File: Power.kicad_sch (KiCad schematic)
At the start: 19 parts, among them U1 SY8089AAAC, U2 SGM2048-ADJXTEK8G/TR

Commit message: Global label modified
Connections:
- net +3V3 renamed +3V3 main
- net +3V3 main: no longer C8.1, R7.2, U2.1 (OUT), U2.2 (OUT)
- new net +3V3 sens: C8.1, R7.2, U2.1 (OUT), U2.2 (OUT)
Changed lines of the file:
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@@
-		)
-	)
-	(label "Vout-Sens"
-		(at 214.63 96.52 0)
-		(effects
-			(font
-				(size 1.27 1.27)
-			)
-			(justify left bottom)
-		)
-	)
-	(label "Vout-Main"
-		(at 218.44 46.99 0)
-		(effects
-			(font
-				(size 1.27 1.27)
-			)
-			(justify left bottom)
 		)
 	)
@@
 			)
 		)
-		(property "Value" "+3V3"
+		(property "Value" "+3V3 main"
 			(at 218.44 48.2599 90)
 			(show_name no)
@@
 			)
 		)
-		(property "Value" "+3V3"
+		(property "Value" "+3V3 sens"
 			(at 217.17 99.0599 90)
 			(show_name no)

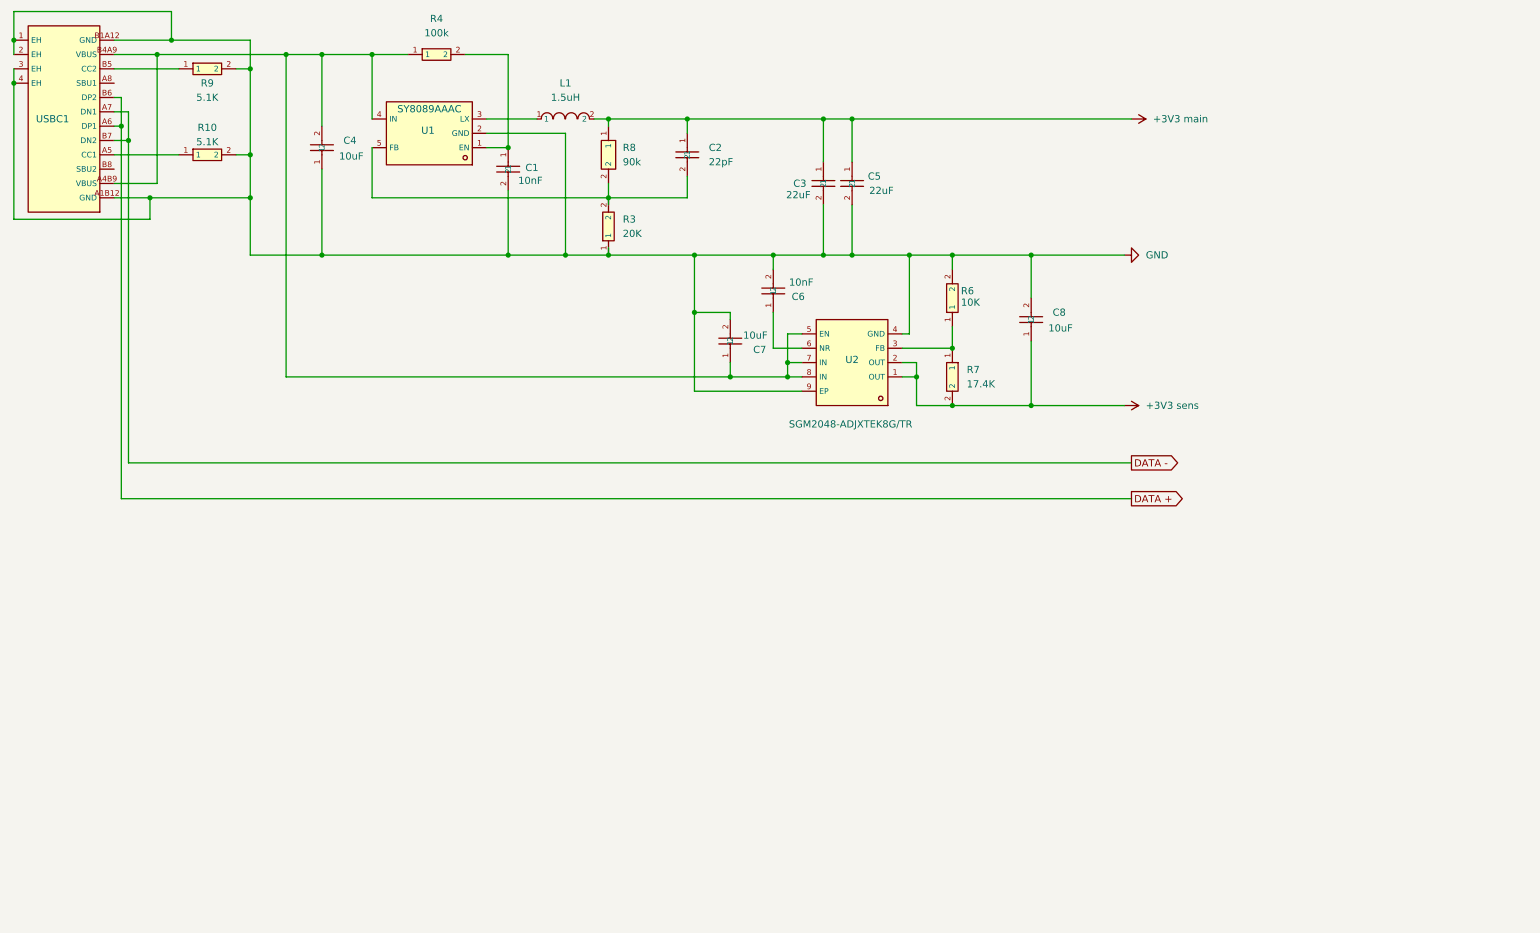
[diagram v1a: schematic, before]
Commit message: Error correction
Corrected resistor value for LDO and added slow rise resistor and capacitorfor LDO
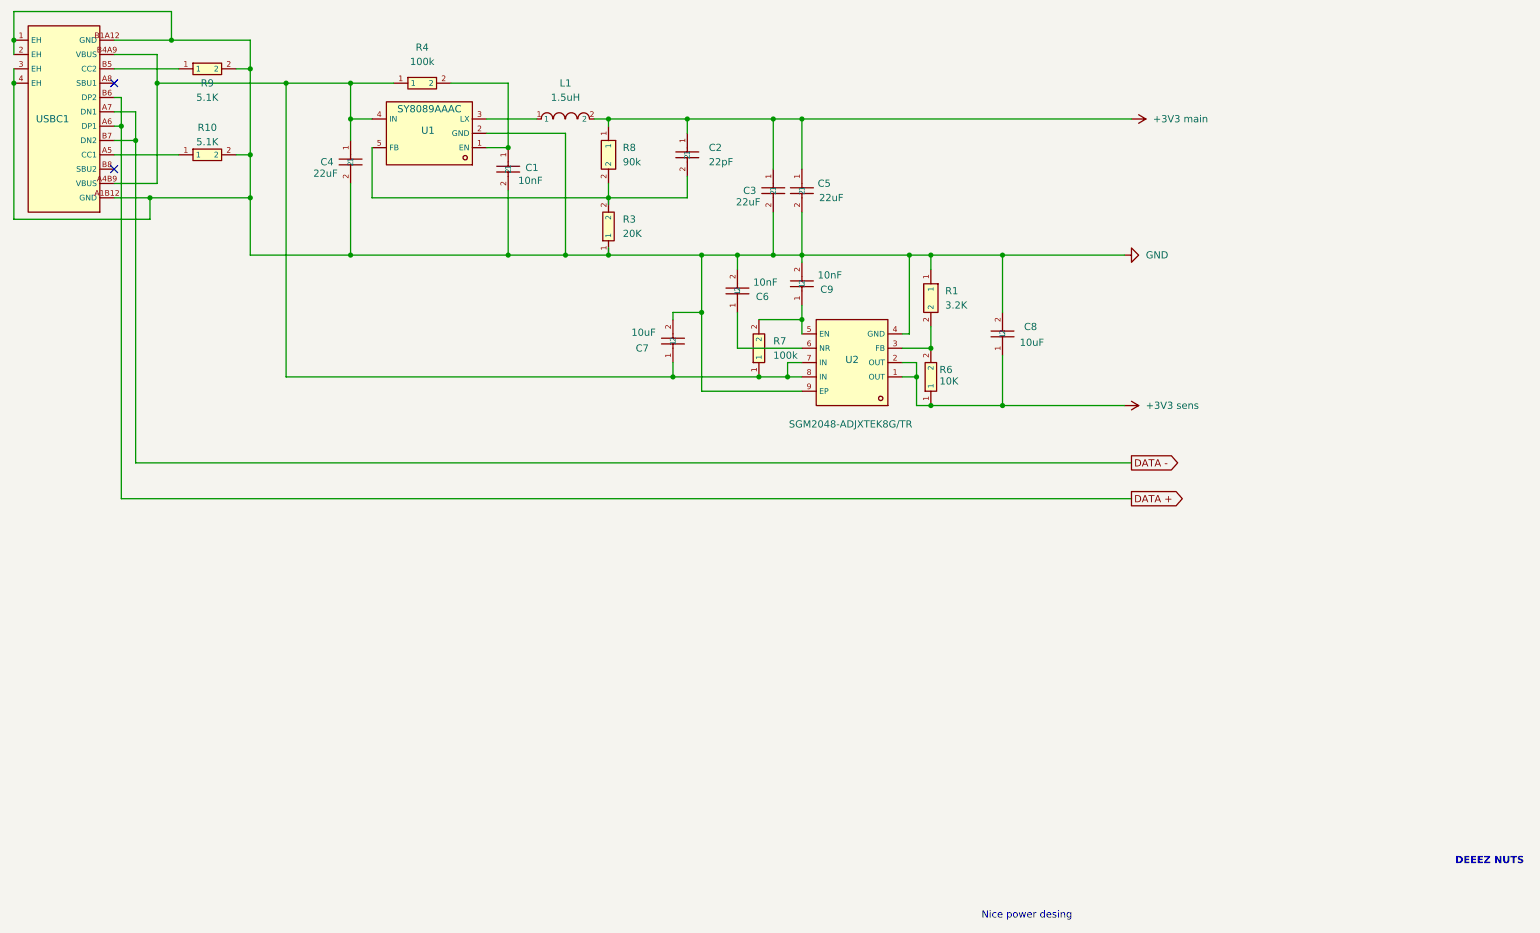
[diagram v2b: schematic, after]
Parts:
- removed C4: 10uF, lcsc_footprints:C1713_C0805, symbol lcsc_imported:10uF_(106)_±10%_16V
- removed R7: 17.4K, lcsc_footprints:C19796_R0805, symbol lcsc_imported:17_4KΩ_(1742)_±1%
- added C4: 22uF, lcsc_footprints:C109448_C0603, symbol lcsc_imported:CC0603MRX5R5BB226
- added C9: 10nF, lcsc_footprints:C1589_C0603, symbol lcsc_imported:10nF_(103)_±10%_50V
- added R1: 3.2K, lcsc_footprints:C705066_R0402, symbol lcsc_imported:RT0402BRD073K2L
- added R7: 100k, lcsc_footprints:C14675_R0603, symbol lcsc_imported:RC0603FR-07100KL
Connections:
- net +3V3 sens: now also R6.1
- net GND: now also C4.2, C9.2, R1.1; no longer R6.2
- net at C7.1, R4.1, U1.4 (IN)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: now also C4.1, R7.1; no longer U2.5 (EN)
- net at U2.3 (FB): now also R6.2, R1.2; no longer R6.1
- new net: C9.1, R7.2, U2.5 (EN)
- no-connect marks 0 -> 2
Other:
- note added: "DEEEZ NUTS"
- note added: "Nice power desing"
- moved on the sheet: C3, C5, C6, C7, C8, R4, R6

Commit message: Final Routing
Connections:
- net +3V3 main renamed +3.3V_Main
- net +3V3 sens renamed +3.3V_Sensors
- net DATA + renamed USB_Data+
- net DATA - renamed USB_Data-
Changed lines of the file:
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@@
 		)
 	)
-	(global_label "DATA +"
+	(hierarchical_label "USB_Data-"
 		(shape output)
-		(at 214.63 115.57 0)
-		(fields_autoplaced yes)
+		(at 214.63 109.22 0)
 		(effects
 			(font
@@
 			(justify left)
 		)
-		(property "Intersheetrefs" "${INTERSHEET_REFS}"
-			(at 224.57 115.57 0)
-			(hide yes)
-			(show_name no)
-			(do_not_autoplace no)
-			(effects
-				(font
-					(size 1.27 1.27)
-				)
-				(justify left)
-			)
-		)
-	)
-	(global_label "DATA -"
+	)
+	(hierarchical_label "+3.3V_Main"
 		(shape output)
-		(at 214.63 109.22 0)
-		(fields_autoplaced yes)
+		(at 214.63 48.26 0)
 		(effects
 			(font
@@
 			(justify left)
 		)
-		(property "Intersheetrefs" "${INTERSHEET_REFS}"
-			(at 224.57 109.22 0)
-			(hide yes)
-			(show_name no)
-			(do_not_autoplace no)
-			(effects
-				(font
-					(size 1.27 1.27)
-				)
-				(justify left)
-			)
-		)
-	)
-	(symbol
-		(lib_id "power:+3V3")
-		(at 214.63 48.26 270)
-		(unit 1)
-		(body_style 1)
-		(exclude_from_sim no)
-		(in_bom yes)
-		(on_board yes)
-		(in_pos_files yes)
-		(dnp no)
-		(fields_autoplaced yes)
-		(property "Reference" "#PWR01"
-			(at 210.82 48.26 0)
-			(hide yes)
-			(show_name no)
-			(do_not_autoplace no)
-			(effects
-				(font
-					(size 1.27 1.27)
-				)
-			)
-		)
-		(property "Value" "+3V3 main"
-			(at 218.44 48.2599 90)
-			(show_name no)
-			(do_not_autoplace no)
-			(effects
-				(font
-					(size 1.27 1.27)
-				)
-				(justify left)
-			)
-		)
-		(property "Footprint" ""
-			(at 214.63 48.26 0)
-			(hide yes)
-			(show_name no)
-			(do_not_autoplace no)
-			(effects
-				(font
-					(size 1.27 1.27)
-				)
-			)
-		)
-		(property "Datasheet" ""
-			(at 214.63 48.26 0)
-			(hide yes)
-			(show_name no)
-			(do_not_autoplace no)
-			(effects
-				(font
-					(size 1.27 1.27)
-				)
-			)
-		)
-		(property "Description" "Power symbol creates a global label with name \"+3V3\""
-			(at 214.63 48.26 0)
-			(hide yes)
-			(show_name no)
-			(do_not_autoplace no)
-			(effects
-				(font
-					(size 1.27 1.27)
-				)
-			)
-		)
-		(pin "1"
-		)
-		(instances
-			(project "SuperNicePCB"
-				(path "/794e52b0-48ac-4476-a221-597be743d898/df5ae8a1-734c-498d-8b76-baff75009c73"
-					(reference "#PWR01")
-					(unit 1)
-				)
-			)
-			(project "Power"
-				(path "/9738fb9c-9ff2-40ed-bfe8-52a4b3df91ac"
-					(reference "#PWR01")
-					(unit 1)
-				)
-			)
+	)
+	(hierarchical_label "+3.3V_Sensors"
+		(shape output)
+		(at 213.36 99.06 0)
+		(effects
+			(font
+				(size 1.27 1.27)
+			)
+			(justify left)
+		)
+	)
+	(hierarchical_label "USB_Data+"
+		(shape output)
+		(at 214.63 115.57 0)
+		(effects
+			(font
+				(size 1.27 1.27)
+			)
+			(justify left)
 		)
 	)
@@
 	)
 	(symbol
-		(lib_id "power:+3V3")
-		(at 213.36 99.06 270)
-		(unit 1)
-		(body_style 1)
-		(exclude_from_sim no)
-		(in_bom yes)
-		(on_board yes)
-		(in_pos_files yes)
-		(dnp no)
-		(fields_autoplaced yes)
-		(property "Reference" "#PWR03"
-			(at 209.55 99.06 0)
-			(hide yes)
-			(show_name no)
-			(do_not_autoplace no)
-			(effects
-				(font
-					(size 1.27 1.27)
-				)
-			)
-		)
-		(property "Value" "+3V3 sens"
-			(at 217.17 99.0599 90)
-			(show_name no)
-			(do_not_autoplace no)
-			(effects
-				(font
-					(size 1.27 1.27)
-				)
-				(justify left)
-			)
-		)
-		(property "Footprint" ""
-			(at 213.36 99.06 0)
-			(hide yes)
-			(show_name no)
-			(do_not_autoplace no)
-			(effects
-				(font
-					(size 1.27 1.27)
-				)
-			)
-		)
-		(property "Datasheet" ""
-			(at 213.36 99.06 0)
-			(hide yes)
-			(show_name no)
-			(do_not_autoplace no)
-			(effects
-				(font
-					(size 1.27 1.27)
-				)
-			)
-		)
-		(property "Description" "Power symbol creates a global label with name \"+3V3\""
-			(at 213.36 99.06 0)
-			(hide yes)
-			(show_name no)
-			(do_not_autoplace no)
-			(effects
-				(font
-					(size 1.27 1.27)
-				)
-			)
-		)
-		(pin "1"
-		)
-		(instances
-			(project "SuperNicePCB"
-				(path "/794e52b0-48ac-4476-a221-597be743d898/df5ae8a1-734c-498d-8b76-baff75009c73"
-					(reference "#PWR03")
-					(unit 1)
-				)
-			)
-			(project "Power"
-				(path "/9738fb9c-9ff2-40ed-bfe8-52a4b3df91ac"
-					(reference "#PWR03")
-					(unit 1)
-				)
-			)
-		)
-	)
-	(symbol
 		(lib_id "lcsc_imported:CC0603MRX5R5BB226")
 		(at 151.13 60.96 270)
@@
 		)
 	)
+	(embedded_fonts no)
 )

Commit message: Changed footprint of the test point
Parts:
- renumbered C3 to C10, C5 to C11, C9 to C12, C8 to C13, C4 to C5, C1 to C6, C2 to C8, C6 to C9, R9 to R2, R10 to R3, R8 to R5, R3 to R6, R1 to R8, R6 to R9, U1 to U2, U2 to U3
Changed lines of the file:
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@@
 		(dnp no)
 		(fields_autoplaced yes)
-		(property "Reference" "R8"
+		(property "Reference" "R5"
 			(at 124.46 53.3399 90)
 			(show_name no)
@@
 			(project "SuperNicePCB"
 				(path "/794e52b0-48ac-4476-a221-597be743d898/df5ae8a1-734c-498d-8b76-baff75009c73"
-					(reference "R8")
+					(reference "R5")
 					(unit 1)
 				)
@@
 		(in_pos_files yes)
 		(dnp no)
-		(property "Reference" "C4"
+		(property "Reference" "C5"
 			(at 70.866 55.88 90)
 			(show_name no)
@@
 			(project "SuperNicePCB"
 				(path "/794e52b0-48ac-4476-a221-597be743d898/df5ae8a1-734c-498d-8b76-baff75009c73"
-					(reference "C4")
+					(reference "C5")
 					(unit 1)
 				)
@@
 		(in_pos_files yes)
 		(dnp no)
-		(property "Reference" "C5"
+		(property "Reference" "C11"
 			(at 159.004 59.69 90)
 			(show_name no)
@@
 			(project "SuperNicePCB"
 				(path "/794e52b0-48ac-4476-a221-597be743d898/df5ae8a1-734c-498d-8b76-baff75009c73"
-					(reference "C5")
+					(reference "C11")
 					(unit 1)
 				)
@@
 		(dnp no)
 		(fields_autoplaced yes)
-		(property "Reference" "R3"
+		(property "Reference" "R6"
 			(at 124.46 66.0399 90)
 			(show_name no)
@@
 			(project "SuperNicePCB"
 				(path "/794e52b0-48ac-4476-a221-597be743d898/df5ae8a1-734c-498d-8b76-baff75009c73"
-					(reference "R3")
+					(reference "R6")
 					(unit 1)
 				)
@@
 		(dnp no)
 		(fields_autoplaced yes)
-		(property "Reference" "C2"
+		(property "Reference" "C8"
 			(at 139.7 53.3399 90)
 			(show_name no)
@@
 			(project "SuperNicePCB"
 				(path "/794e52b0-48ac-4476-a221-597be743d898/df5ae8a1-734c-498d-8b76-baff75009c73"
-					(reference "C2")
+					(reference "C8")
 					(unit 1)
 				)
@@
 		(in_pos_files yes)
 		(dnp no)
-		(property "Reference" "U2"
+		(property "Reference" "U3"
 			(at 165.1 90.932 0)
 			(show_name no)
@@
 			(project "SuperNicePCB"
 				(path "/794e52b0-48ac-4476-a221-597be743d898/df5ae8a1-734c-498d-8b76-baff75009c73"
-					(reference "U2")
+					(reference "U3")
 					(unit 1)
 				)
@@
 		(in_pos_files yes)
 		(dnp no)
-		(property "Reference" "C1"
+		(property "Reference" "C6"
 			(at 107.188 56.896 90)
 			(show_name no)
@@
 			(project "SuperNicePCB"
 				(path "/794e52b0-48ac-4476-a221-597be743d898/df5ae8a1-734c-498d-8b76-baff75009c73"
-					(reference "C1")
+					(reference "C6")
 					(unit 1)
 				)
@@
 		(in_pos_files yes)
 		(dnp no)
-		(property "Reference" "R10"
+		(property "Reference" "R3"
 			(at 50.8 49.784 0)
 			(show_name no)
@@
 			(project "SuperNicePCB"
 				(path "/794e52b0-48ac-4476-a221-597be743d898/df5ae8a1-734c-498d-8b76-baff75009c73"
-					(reference "R10")
+					(reference "R3")
 					(unit 1)
 				)
@@
 		(in_pos_files yes)
 		(dnp no)
-		(property "Reference" "C9"
+		(property "Reference" "C12"
 			(at 161.798 78.486 90)
 			(show_name no)
@@
 			(project "SuperNicePCB"
 				(path "/794e52b0-48ac-4476-a221-597be743d898/df5ae8a1-734c-498d-8b76-baff75009c73"
-					(reference "C9")
+					(reference "C12")
 					(unit 1)
 				)
@@
 		(in_pos_files yes)
 		(dnp no)
-		(property "Reference" "U1"
+		(property "Reference" "U2"
 			(at 89.916 50.292 0)
 			(show_name no)
@@
 			(project "SuperNicePCB"
 				(path "/794e52b0-48ac-4476-a221-597be743d898/df5ae8a1-734c-498d-8b76-baff75009c73"
-					(reference "U1")
+					(reference "U2")
 					(unit 1)
 				)
@@
 		(in_pos_files yes)
 		(dnp no)
-		(property "Reference" "C6"
+		(property "Reference" "C9"
 			(at 150.368 79.756 90)
 			(show_name no)
@@
 			(project "SuperNicePCB"
 				(path "/794e52b0-48ac-4476-a221-597be743d898/df5ae8a1-734c-498d-8b76-baff75009c73"
-					(reference "C6")
+					(reference "C9")
 					(unit 1)
 				)
@@
 		(in_pos_files yes)
 		(dnp no)
-		(property "Reference" "C8"
+		(property "Reference" "C13"
 			(at 195.58 85.0899 90)
 			(show_name no)
@@
 			(project "SuperNicePCB"
 				(path "/794e52b0-48ac-4476-a221-597be743d898/df5ae8a1-734c-498d-8b76-baff75009c73"
-					(reference "C8")
+					(reference "C13")
 					(unit 1)
 				)
@@
 		(dnp no)
 		(fields_autoplaced yes)
-		(property "Reference" "R1"
+		(property "Reference" "R8"
 			(at 181.61 78.7399 90)
 			(show_name no)
@@
 			(project "SuperNicePCB"
 				(path "/794e52b0-48ac-4476-a221-597be743d898/df5ae8a1-734c-498d-8b76-baff75009c73"
-					(reference "R1")
+					(reference "R8")
 					(unit 1)
 				)
@@
 		(dnp no)
 		(fields_autoplaced yes)
-		(property "Reference" "#PWR02"
+		(property "Reference" "#PWR012"
 			(at 219.71 72.39 0)
 			(hide yes)
@@
 			(project "SuperNicePCB"
 				(path "/794e52b0-48ac-4476-a221-597be743d898/df5ae8a1-734c-498d-8b76-baff75009c73"
-					(reference "#PWR02")
+					(reference "#PWR012")
 					(unit 1)
 				)
@@
 		(in_pos_files yes)
 		(dnp no)
-		(property "Reference" "R9"
+		(property "Reference" "R2"
 			(at 50.8 41.91 0)
 			(show_name no)
@@
 			(project "SuperNicePCB"
 				(path "/794e52b0-48ac-4476-a221-597be743d898/df5ae8a1-734c-498d-8b76-baff75009c73"
-					(reference "R9")
+					(reference "R2")
 					(unit 1)
 				)
@@
 		(in_pos_files yes)
 		(dnp no)
-		(property "Reference" "C3"
+		(property "Reference" "C10"
 			(at 145.796 60.96 90)
 			(show_name no)
@@
 			(project "SuperNicePCB"
 				(path "/794e52b0-48ac-4476-a221-597be743d898/df5ae8a1-734c-498d-8b76-baff75009c73"
-					(reference "C3")
+					(reference "C10")
 					(unit 1)
 				)
@@
 		(in_pos_files yes)
 		(dnp no)
-		(property "Reference" "R6"
+		(property "Reference" "R9"
 			(at 180.594 92.71 90)
 			(show_name no)
@@
 			(project "SuperNicePCB"
 				(path "/794e52b0-48ac-4476-a221-597be743d898/df5ae8a1-734c-498d-8b76-baff75009c73"
-					(reference "R6")
-					(unit 1)
-				)
+					(reference "R9")
+					(unit 1)
+				)

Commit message: Rerouting
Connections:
- net +3.3V_Main renamed 3V3_MCU
- net +3.3V_Sensors renamed 3V3_SENS
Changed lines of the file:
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@@
 		)
 	)
-	(hierarchical_label "+3.3V_Main"
+	(hierarchical_label "3V3_MCU"
 		(shape output)
 		(at 214.63 48.26 0)
@@
 		)
 	)
-	(hierarchical_label "+3.3V_Sensors"
+	(hierarchical_label "3V3_SENS"
 		(shape output)
 		(at 213.36 99.06 0)
@@
 		)
 	)
-	(embedded_fonts no)
 )

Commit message: Modified power routes/ added test point
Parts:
- added 3.4, 3.5, 3.6: TestPoint, TestPoint:TestPoint_Pad_1.0x1.0mm, symbol Connector:TestPoint
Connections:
- net 3V3_MCU: now also 3.4.1
- net 3V3_SENS: now also 3.6.1
- net GND: now also 3.5.1
